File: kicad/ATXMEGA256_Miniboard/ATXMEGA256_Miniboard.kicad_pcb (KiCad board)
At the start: 4 copper layers, 55 x 102 mm, 49 parts, among them J1 10118192-0001LF, J10 2x5 Goldpin Socket, J11 2x5 Goldpin Socket, J12 2x5 Goldpin Socket, J13 2x5 Goldpin Socket, J14 2x5 Goldpin Socket, J15 2x5 Goldpin Socket, J2 2x5 IDC Socket, J3 2x3 IDC Socket, J4 1x3 Goldpin Header, J5 1x2 Goldpin Header, J6 1x2 Goldpin Header, J8 1x3 Goldpin Header, J9 1x2 Screw Terminal, Q1 MMFTP3334K, SW1 RESET, U1 ATXMEGA256A3B-AU, U2 MCP1703A-3302E/DB, Y1 32.768 kHz, Y2 16 MHz

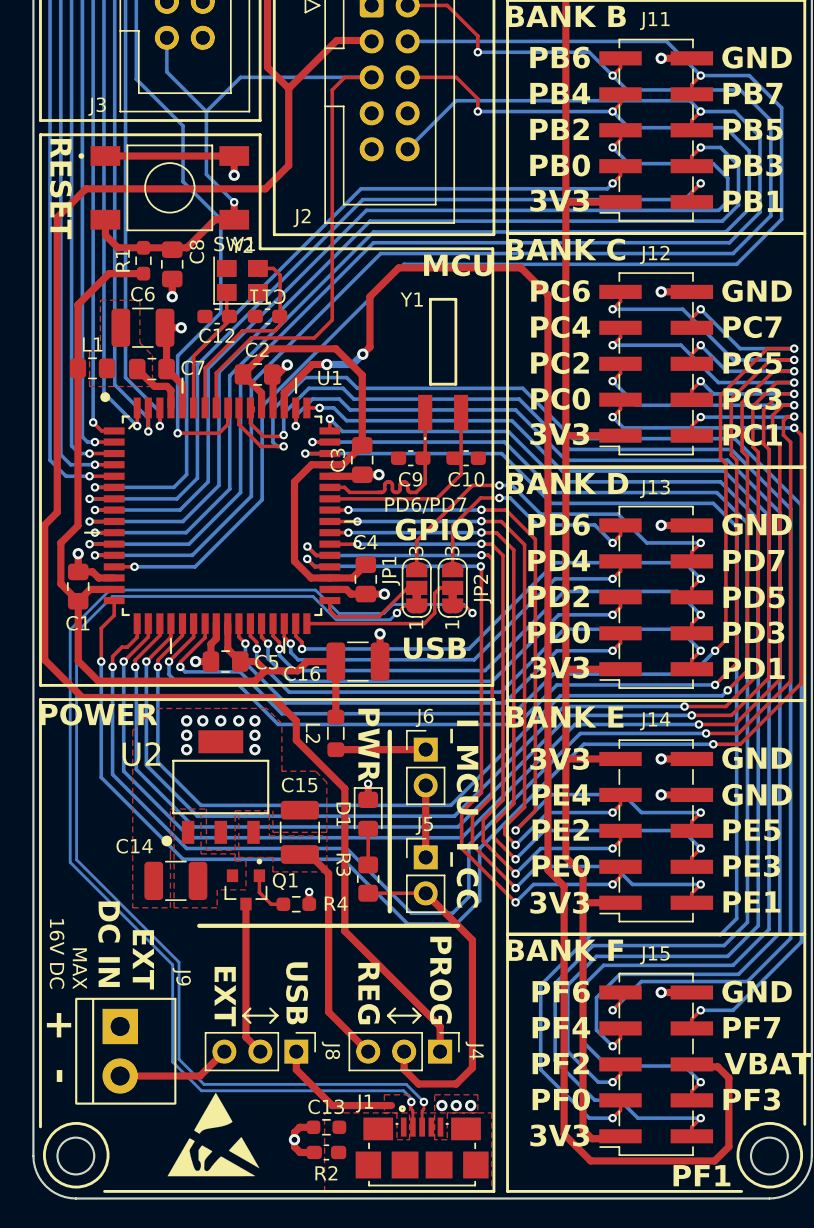
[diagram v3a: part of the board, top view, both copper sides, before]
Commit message: review: rerouting Power i USB
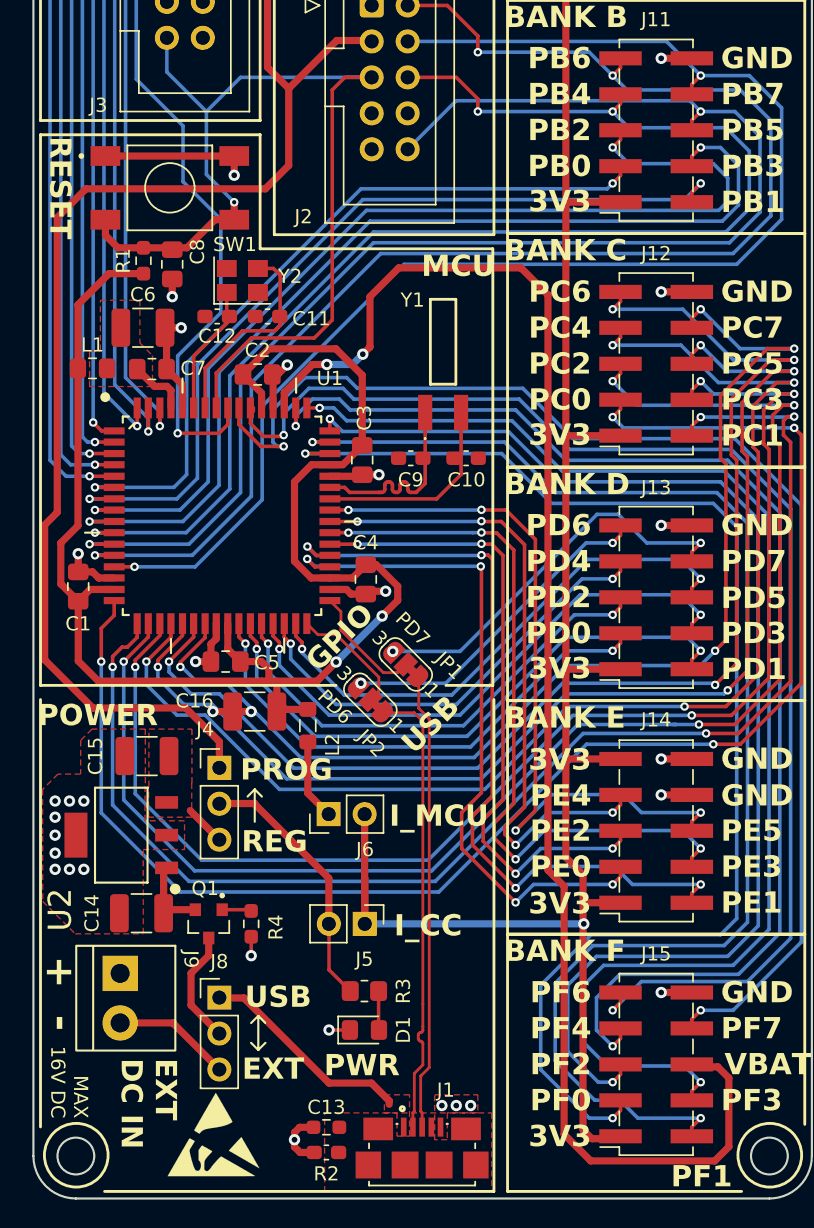
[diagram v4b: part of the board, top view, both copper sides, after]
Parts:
- moved J4 25.4 mm to (181.0, 108.7), turned to 0 degrees
- moved D1 15.2 mm to (191.2, 127.2), turned to 0 degrees
- moved C15 12.1 mm to (175.9, 107.9), turned to 0 degrees
- moved JP2 9.82 mm to (191.7, 103.9), turned to 135 degrees
- moved J6 8.23 mm to (188.7, 112.0), turned to 90 degrees
- moved C16 8.10 mm to (183.5, 104.8), turned to 0 degrees
- moved R3 7.92 mm to (191.2, 124.5), turned to 0 degrees
- moved U2 7.81 mm to (174.1, 113.5), turned to 180 degrees
- moved J8 6.64 mm to (181.0, 125.0), turned to 0 degrees
- moved J5 6.37 mm to (191.3, 119.8), turned to -90 degrees
- moved JP1 5.46 mm to (194.2, 101.4), turned to 135 degrees
- moved J9 3.75 mm to (173.9, 123.2)
- moved Q1 3.56 mm to (180.2, 119.8)
- moved R4 3.47 mm to (183.2, 119.8), turned to -90 degrees
- moved C14 3.33 mm to (175.5, 119.0)
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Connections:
- net Net-(JP1-C) renamed /PD+
- net Net-(JP2-C) renamed /PD-
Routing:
- net /D-: track 85.9 -> 32.3 mm, vias 2 -> 0
- net /D+: track 79.7 -> 32.4 mm, vias 2 -> 0
- net +3V3_EXT: track 122.0 -> 91.4 mm
- net +3V3_IO: track 111.3 -> 132.7 mm, vias 0 -> 1
- net Net-(J4-Pin_3): track 16.3 -> 2.91 mm
- net +3V3_MCU: track 98.2 -> 109.6 mm, vias 0 -> 2
- net +5V_USB: track 9.05 -> 15.3 mm
- net Net-(J4-Pin_2): track 24.8 -> 18.6 mm
- net /PD6: track 18.0 -> 23.4 mm
- net /PC5: track 90.0 -> 84.7 mm
- net Net-(U2-VIN): track 0.00 -> 5.28 mm
- net /PC4: track 97.7 -> 92.8 mm
- net /PD-: track 12.2 -> 8.50 mm
- net /PD0: track 33.1 -> 36.5 mm
- net /PC2: track 99.8 -> 103.1 mm
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- removed copper zone on F.Cu, net Net-(U2-VIN)
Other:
- board text removed: "PD6/PD7"
